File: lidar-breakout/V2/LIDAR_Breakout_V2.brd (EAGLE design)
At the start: 36.5 x 88 mm, 82 parts, among them P1 MOLEX 0436500200, X1 TSX-3225 16.0000MF18X-AC0

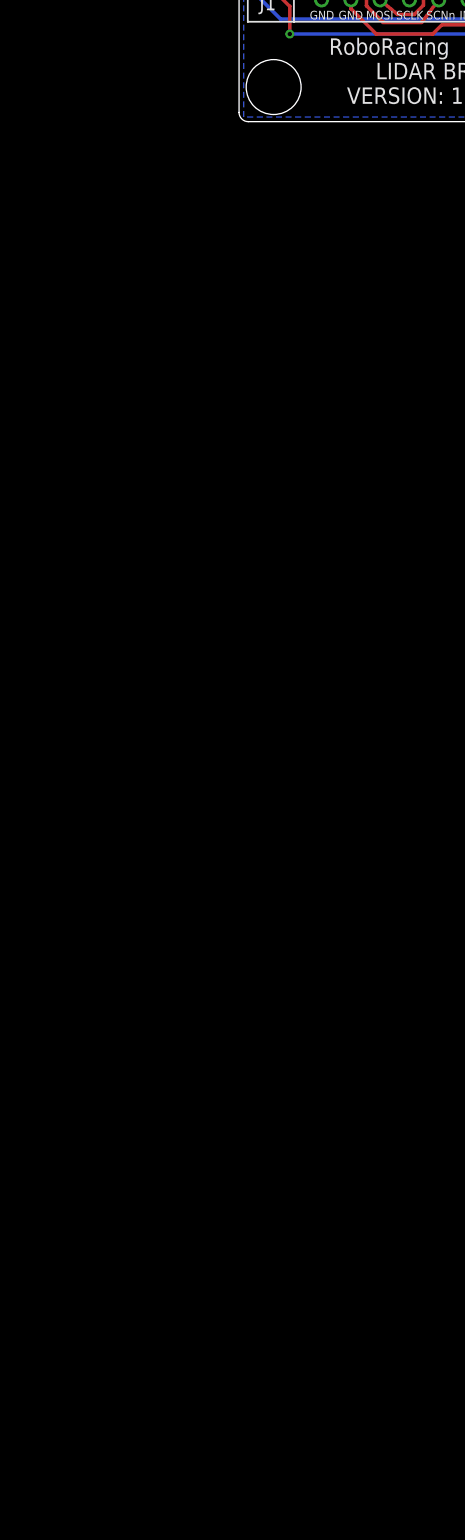
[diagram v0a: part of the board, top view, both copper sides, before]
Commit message: Switched LED directions, Fixed I2C pulled resistor
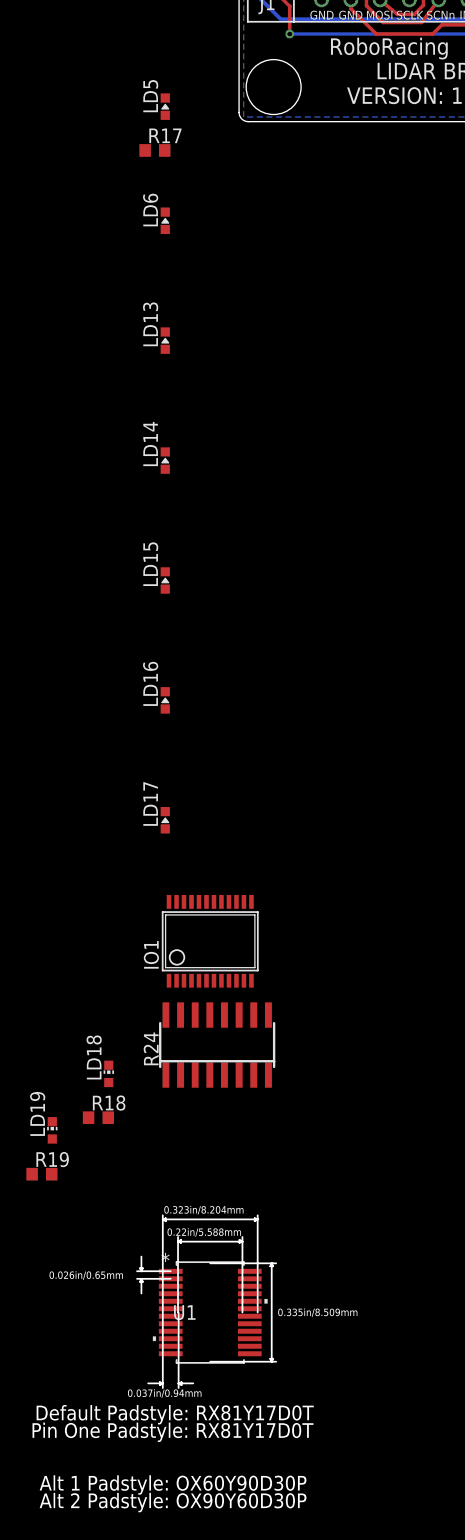
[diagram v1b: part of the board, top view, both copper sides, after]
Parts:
- added IO1: PCA9555DB, micro-philips:SSOP24
- added LD13, LD14, LD15, LD16, LD17, LD5, LD6: RED, RoboJackets-LEDs:CHIP-LED0603
- added LD18, LD19: GREEN, led:CHIP-LED0603
- added R17, R18, R19: 1 kΩ, rcl:R0603
- added R24: 2NBS16-8, resistor-bourns:SO16
- added U1: PCA9548ADBR, PCA9548ADBR:DB24
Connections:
- new net COMM_ERR: R17.1
- new net LDR2_ERR: LD13.A, R24.13
- new net LDR6_ERR: LD14.A, LD15.A, LD16.A, LD17.A, LD6.A, R24.10, R24.11, R24.12, R24.14, R24.9
- new net N$10: LD15.C
- new net N$11: LD18.A, R18.1
- new net N$12: LD19.A, R19.1
- new net N$16: LD16.C
- new net N$18: LD14.C
- new net N$19: LD13.C
- new net N$20: IO1.13, R24.1
- new net N$21: IO1.14, R24.2
- new net N$22: IO1.15, R24.3
- new net N$24: IO1.16, R24.4
- new net N$25: IO1.17, R24.5
- new net N$26: IO1.18, R24.6
- new net N$27: IO1.19, R24.7
- new net N$28: IO1.20, R24.8
- new net N$9: LD5.A, R17.2
- new net VCC: U1.24
- net GND: now also IO1.12, LD17.C, LD18.C, LD19.C, LD5.C, LD6.C, U1.12
- net SCL: now also IO1.22
- net SDA: now also IO1.23
- net VCC_1: now also R19.2
- net VCC_2: now also IO1.24, R18.2
